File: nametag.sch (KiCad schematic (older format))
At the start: 116 parts, among them P1 ISP, Q1 2N7002, Q2 2N7002, Q3 2N7002, Q4 2N7002, Q5 2N7002, U1 ATTINY13-SS

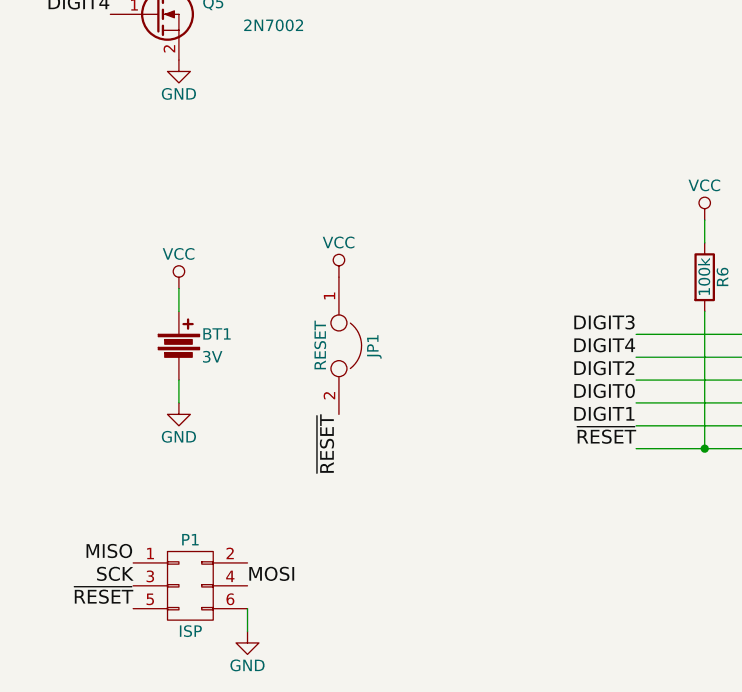
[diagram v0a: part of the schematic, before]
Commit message: Fixed reset button rail mismatch Added missing traces (GND) Replaced reset button by 4-pin standard part
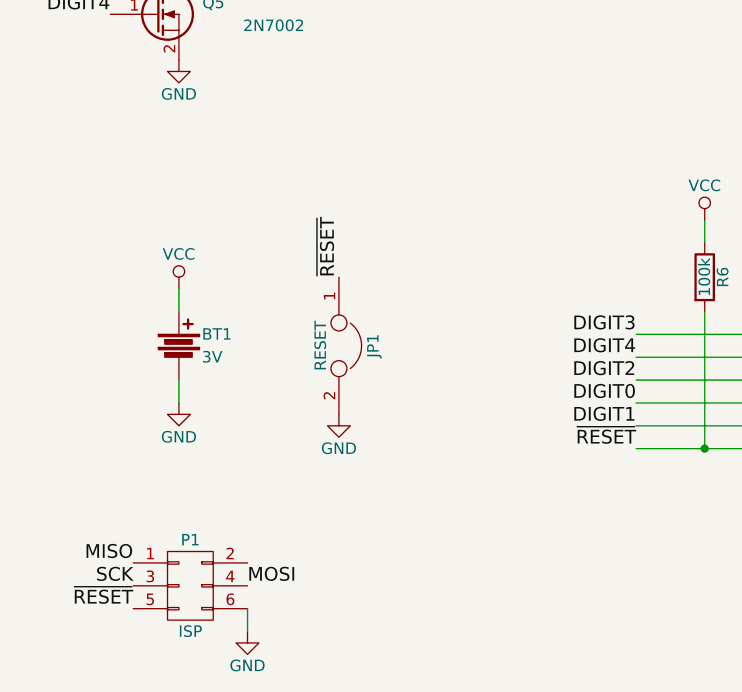
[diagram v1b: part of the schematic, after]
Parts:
- JP1: footprint Pin_Headers:Pin_Header_Straight_1x02 -> Buttons_Switches_ThroughHole:SW_PUSH_SMALL
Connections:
- net GND: now also JP1.2
- net VCC: no longer JP1.1
- net ~RESET: now also JP1.1; no longer JP1.2
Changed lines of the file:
@@
 Text Label 4400 5300 1    60   ~ 0
 MOSI
-Text Label 2300 6150 3    60   ~ 0
+Text Label 2300 5550 1    60   ~ 0
 ~RESET
-$Comp
-L VCC #PWR017
-U 1 1 570E89EE
-P 2300 5550
-F 0 "#PWR017" H 2300 5400 50  0001 C CNN
-F 1 "VCC" H 2300 5700 50  0000 C CNN
-F 2 "" H 2300 5550 50  0000 C CNN
-F 3 "" H 2300 5550 50  0000 C CNN
-	1    2300 5550
-	1    0    0    -1
-$EndComp
 $Comp
 L JUMPER JP1
@@
 F 0 "JP1" H 2300 6000 50  0000 C CNN
 F 1 "RESET" H 2300 5770 50  0000 C CNN
-F 2 "Pin_Headers:Pin_Header_Straight_1x02" H 2300 5850 50  0001 C CNN
+F 2 "Buttons_Switches_ThroughHole:SW_PUSH_SMALL" H 2300 5850 50  0001 C CNN
 F 3 "" H 2300 5850 50  0000 C CNN
 	1    2300 5850
@@
 Wire Wire Line
 	4400 5300 4400 5800
+$Comp
+L GND #PWR017
+U 1 1 5753013C
+P 2300 6150
+F 0 "#PWR017" H 2300 5900 50  0001 C CNN
+F 1 "GND" H 2300 6000 50  0000 C CNN
+F 2 "" H 2300 6150 50  0000 C CNN
+F 3 "" H 2300 6150 50  0000 C CNN
+	1    2300 6150
+	1    0    0    -1
+$EndComp
 $EndSCHEMATC

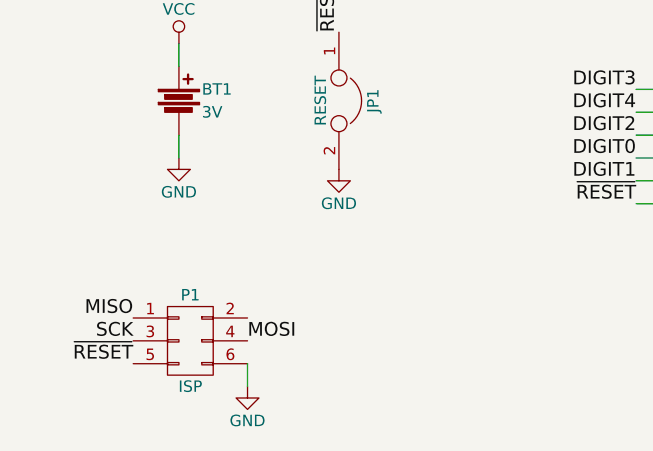
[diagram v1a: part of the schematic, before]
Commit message: Connected Vcc to ISP header Better GND routing in layout
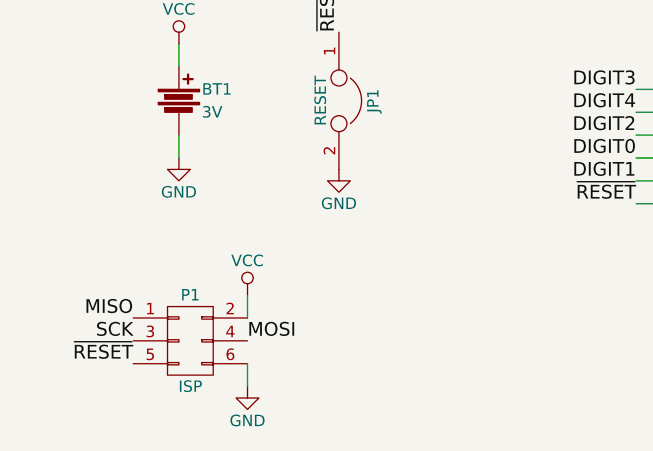
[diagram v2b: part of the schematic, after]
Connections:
- net VCC: now also P1.2 (P2)
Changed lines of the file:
@@
 	1    0    0    -1
 $EndComp
+$Comp
+L VCC #PWR?
+U 1 1 575A755F
+P 1900 6700
+F 0 "#PWR?" H 1900 6550 50  0001 C CNN
+F 1 "VCC" H 1900 6850 50  0000 C CNN
+F 2 "" H 1900 6700 50  0000 C CNN
+F 3 "" H 1900 6700 50  0000 C CNN
+	1    1900 6700
+	1    0    0    -1
+$EndComp
+Wire Wire Line
+	1900 6700 1900 6800
 $EndSCHEMATC
